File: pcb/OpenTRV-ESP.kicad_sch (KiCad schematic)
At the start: 62 parts, among them J1 TagConnect_TC2030, J2 I2C, J3 Buttons, J4 Screen, J5 Stepper Motor, P1 USB_C_Plug_USB2.0, Q1 FDN340P, Q2 BSS123, Q3 BSS123, SW1 EN Push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

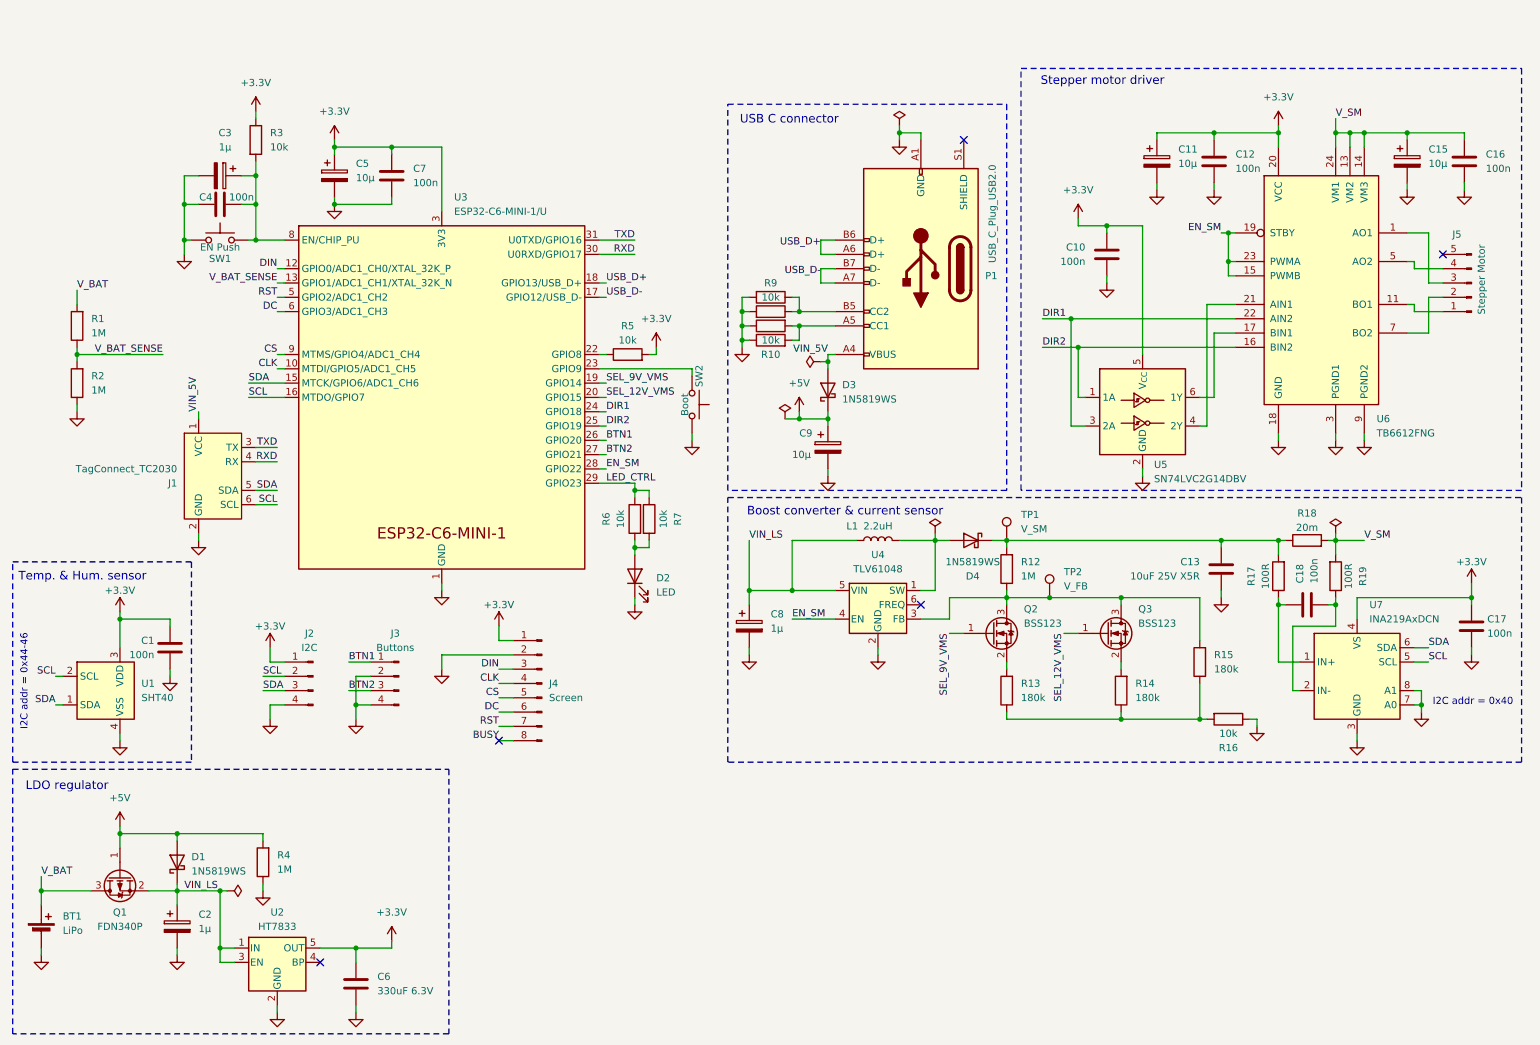
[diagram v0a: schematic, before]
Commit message: Reconnects the stepper driver to the ESP ULP pins
Redoes the board layout and routing.
The temperature sensor is now centered at the bottom of the board.
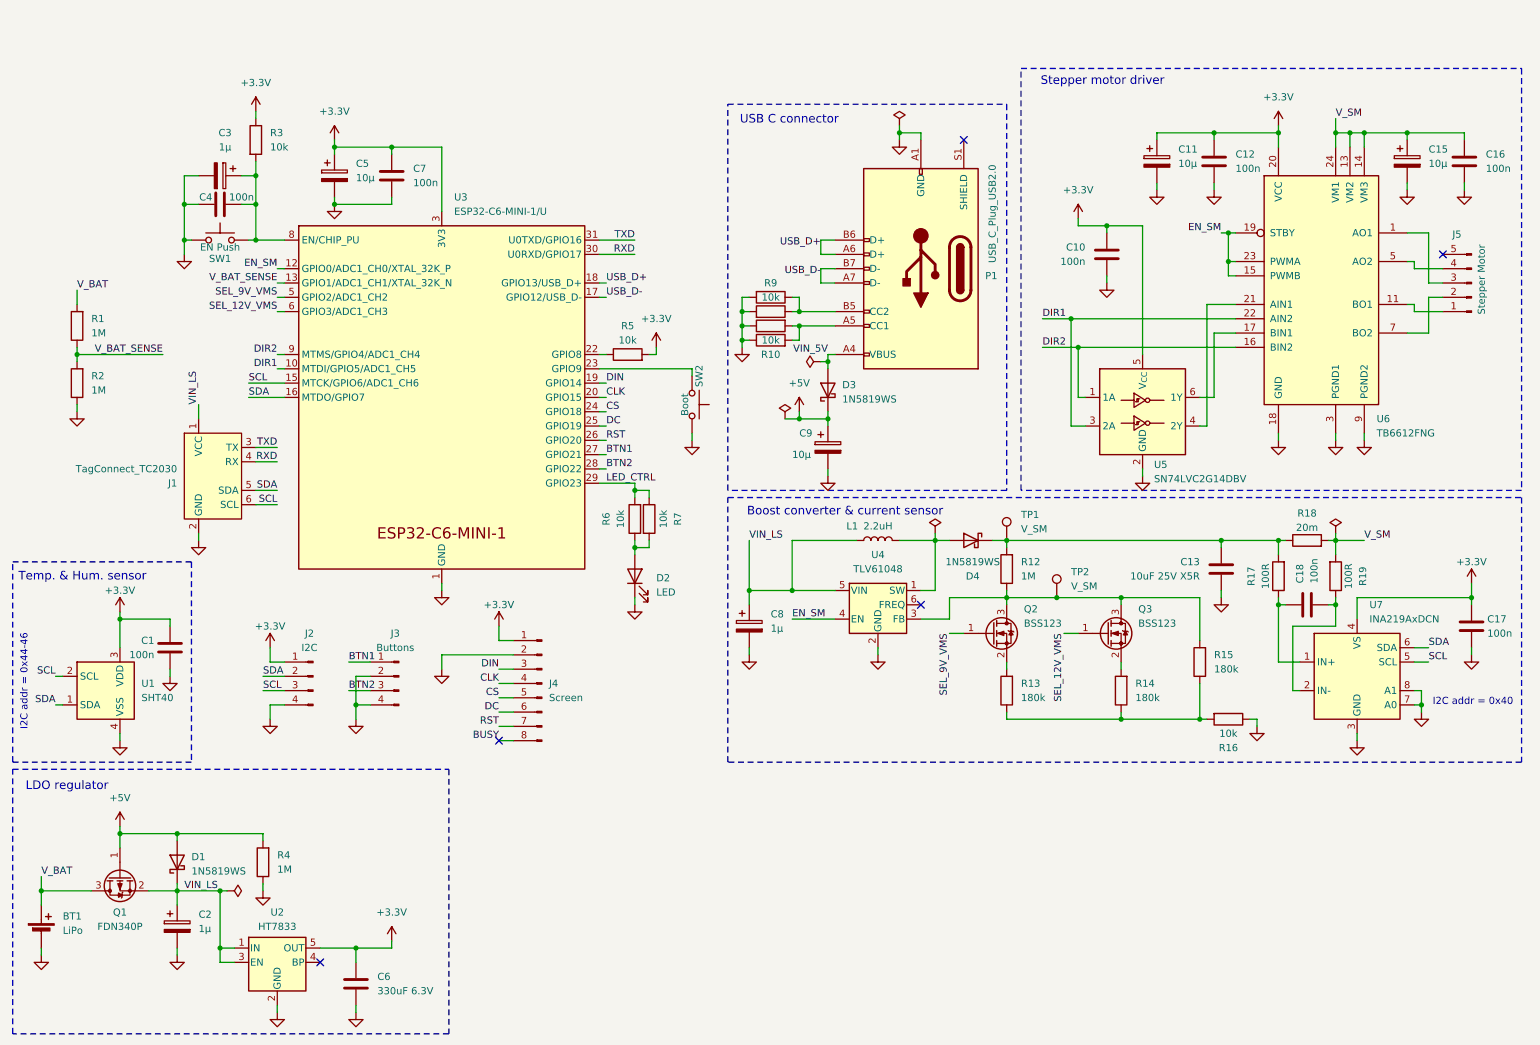
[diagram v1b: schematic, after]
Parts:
- TP2: value V_FB -> V_SM
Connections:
- net BTN1: now also U3.27 (GPIO21); no longer U3.26 (GPIO20)
- net BTN2: now also U3.28 (GPIO22); no longer U3.27 (GPIO21)
- net CLK: now also U3.20 (GPIO15); no longer U3.10 (MTDI/GPIO5/ADC1_CH5)
- net CS: now also U3.24 (GPIO18); no longer U3.9 (MTMS/GPIO4/ADC1_CH4)
- net DC: now also U3.25 (GPIO19); no longer U3.6 (GPIO3/ADC1_CH3)
- net DIN: now also U3.19 (GPIO14); no longer U3.12 (GPIO0/ADC1_CH0/XTAL_32K_P)
- net DIR1: now also U3.10 (MTDI/GPIO5/ADC1_CH5); no longer U3.24 (GPIO18)
- net DIR2: now also U3.9 (MTMS/GPIO4/ADC1_CH4); no longer U3.25 (GPIO19)
- net EN_SM: now also U3.12 (GPIO0/ADC1_CH0/XTAL_32K_P); no longer U3.28 (GPIO22)
- net RST: now also U3.26 (GPIO20); no longer U3.5 (GPIO2/ADC1_CH2)
- net SCL: now also J2.3 (Pin_3), U3.15 (MTCK/GPIO6/ADC1_CH6); no longer J2.2 (Pin_2), U3.16 (MTDO/GPIO7)
- net SDA: now also J2.2 (Pin_2), U3.16 (MTDO/GPIO7); no longer J2.3 (Pin_3), U3.15 (MTCK/GPIO6/ADC1_CH6)
- net SEL_12V_VMS: now also U3.6 (GPIO3/ADC1_CH3); no longer U3.20 (GPIO15)
- net SEL_9V_VMS: now also U3.5 (GPIO2/ADC1_CH2); no longer U3.19 (GPIO14)
- net VIN_5V: no longer J1.1 (VCC)
- net VIN_LS: now also J1.1 (VCC)

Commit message: WIP TMC2300
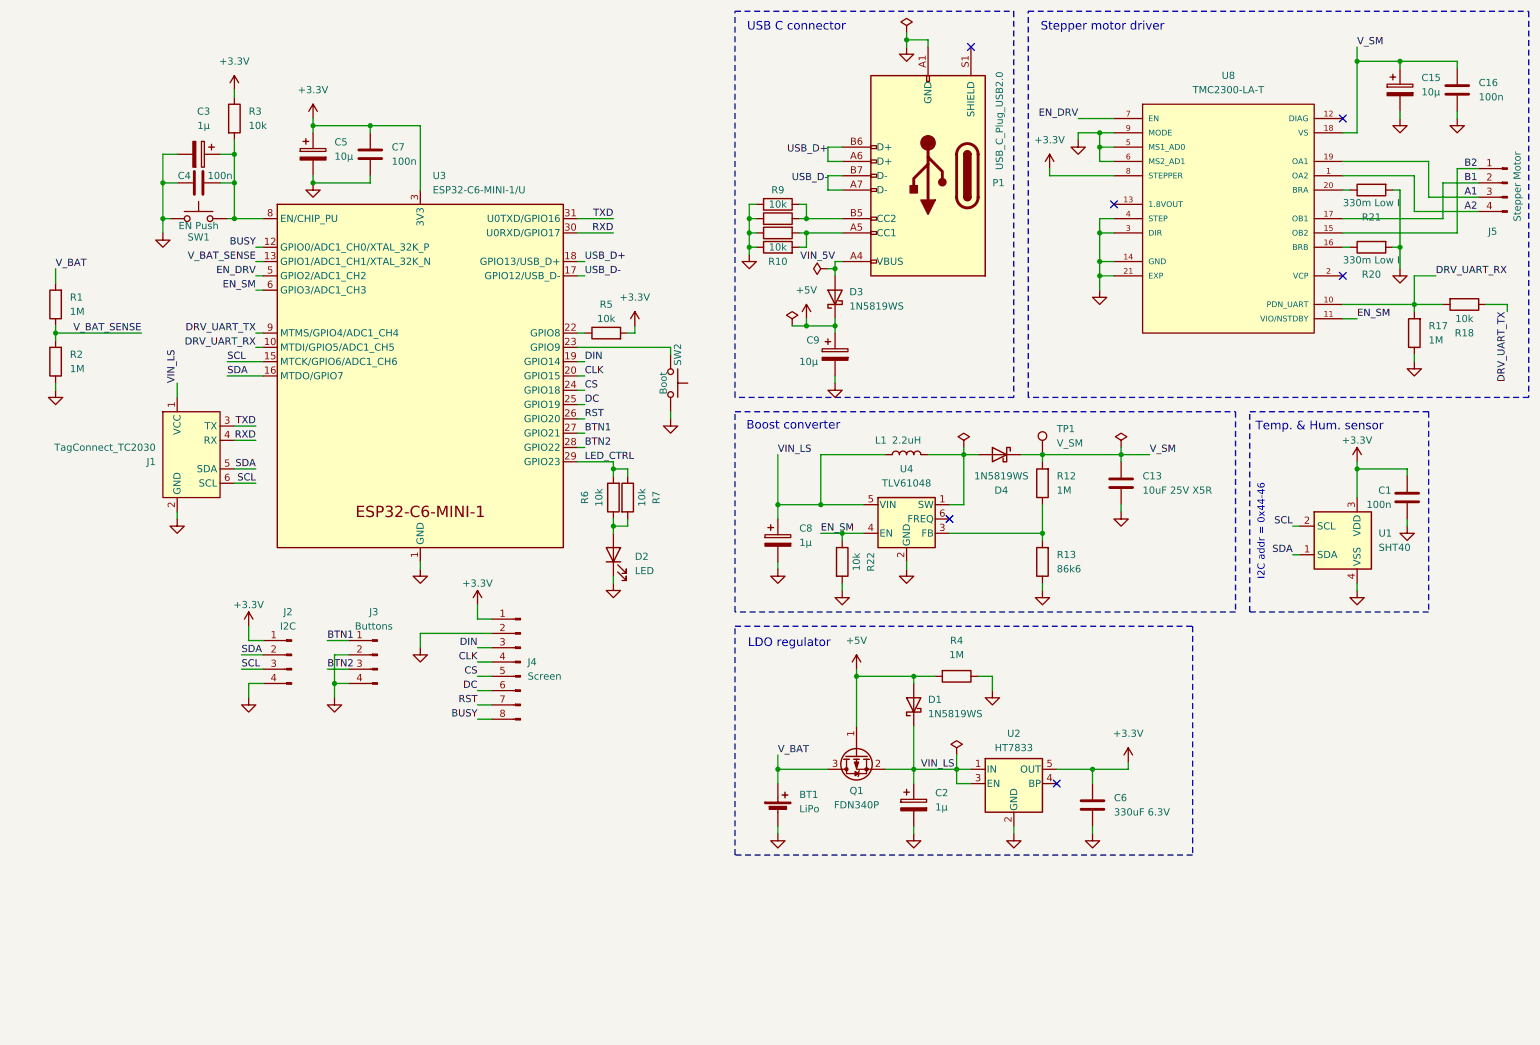
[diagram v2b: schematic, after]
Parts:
- removed C10, C12, C17, C18: 100n, Capacitor_SMD:C_0402_1005Metric, symbol Device:C
- removed C11: 10µ, Capacitor_SMD:C_0603_1608Metric, symbol Device:C_Polarized
- removed J5: Stepper Motor, Connector_JST:JST_XH_B5B-XH-A_1x05_P2.50mm_Vertical, symbol Connector:Conn_01x05_Pin
- removed Q2, Q3: BSS123, Package_TO_SOT_SMD:SOT-23, symbol Transistor_FET:BSS123
- removed R14, R15: 180k, Resistor_SMD:R_0402_1005Metric, symbol Device:R
- removed R16: 10k, Resistor_SMD:R_0402_1005Metric, symbol Device:R
- removed R19: 100R, Resistor_SMD:R_0603_1608Metric, symbol Device:R
- removed TP2: V_SM, TestPoint:TestPoint_Pad_D1.0mm, symbol Connector:TestPoint
- removed U5: SN74LVC2G14DBV, Package_TO_SOT_SMD:SOT-23-6, symbol 74xGxx:SN74LVC2G14DBV
- removed U6: TB6612FNG, Package_SO:SSOP-24_5.3x8.2mm_P0.65mm, symbol Driver_Motor:TB6612FNG
- removed U7: INA219AxDCN, Package_TO_SOT_SMD:SOT-23-8_Handsoldering, symbol Sensor_Energy:INA219AxDCN
- added J5: Stepper Motor, Connector_JST:JST_XH_B4B-XH-A_1x04_P2.50mm_Vertical, symbol Connector:Conn_01x04_Pin
- added R20, R21: 330m Low I, Resistor_SMD:R_1206_3216Metric, symbol Device:R
- added R22: 10k, Resistor_SMD:R_0402_1005Metric, symbol Device:R
- added U8: TMC2300-LA-T, mpiraux:QFN40P300X300X90-21N, symbol TMC2300:TMC2300-LA-T
- R13: value 180k -> 86k6
- R17: value 100R -> 1M; footprint Resistor_SMD:R_0603_1608Metric -> Resistor_SMD:R_0402_1005Metric
- R18: value 20m -> 10k; footprint Resistor_SMD:R_0603_1608Metric -> Resistor_SMD:R_0402_1005Metric
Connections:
- net SEL_12V_VMS is gone; now on net EN_SM: U3.6 (GPIO3/ADC1_CH3)
- net +3.3V: now also U8.8 (STEPPER)
- net BUSY: now also U3.12 (GPIO0/ADC1_CH0/XTAL_32K_P)
- net EN_SM: now also R22.1, U8.11 (VIO/NSTDBY); no longer U3.12 (GPIO0/ADC1_CH0/XTAL_32K_P)
- net GND: now also R13.1, R17.1, R20.2, R21.2, R22.2, U8.14 (GND), U8.21 (EXP), U8.3 (DIR), U8.4 (STEP), U8.5 (MS1_AD0), U8.6 (MS2_AD1), U8.9 (MODE)
- net V_SM: now also C13.1, D4.1 (K), R12.2, TP1.1, U8.18 (VS); no longer R18.2
- net at R12.1, U4.3 (FB): now also R13.2
- net DIR1 renamed DRV_UART_RX
- net DRV_UART_RX: now also R17.2, R18.2, U8.10 (PDN_UART)
- net DIR2 renamed DRV_UART_TX
- net DRV_UART_TX: now also R18.1
- net SEL_9V_VMS renamed EN_DRV
- net EN_DRV: now also U8.7 (EN)
- new net: R20.1, U8.16 (BRB)
- new net: R21.1, U8.20 (BRA)
- new net A1: J5.3 (Pin_3), U8.19 (OA1)
- new net A2: J5.4 (Pin_4), U8.1 (OA2)
- new net B1: J5.2 (Pin_2), U8.17 (OB1)
- new net B2: J5.1 (Pin_1), U8.15 (OB2)
- no-connect marks 5 -> 6
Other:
- note added: "Boost converter"
- note removed: "Boost converter & current sensor"
- note removed: "I2C addr = 0x40"
- moved on the sheet: BT1, C1, C13, C15, C16, C2, C3, C4, C5, C6, C7, C8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
